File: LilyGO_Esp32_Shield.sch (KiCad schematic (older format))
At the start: 45 parts, among them J1 Conn. Flow4, J2 Conn. Flow3, J3 Conn. Flow2, J4 Conn. Flow1, J5 Conn. Pressure, J6 TEMP1, J7 TEMP2, SW1 SW_SPDT, U1 SN74HC14DR, U2 LilyGO_ESP32_TTGO

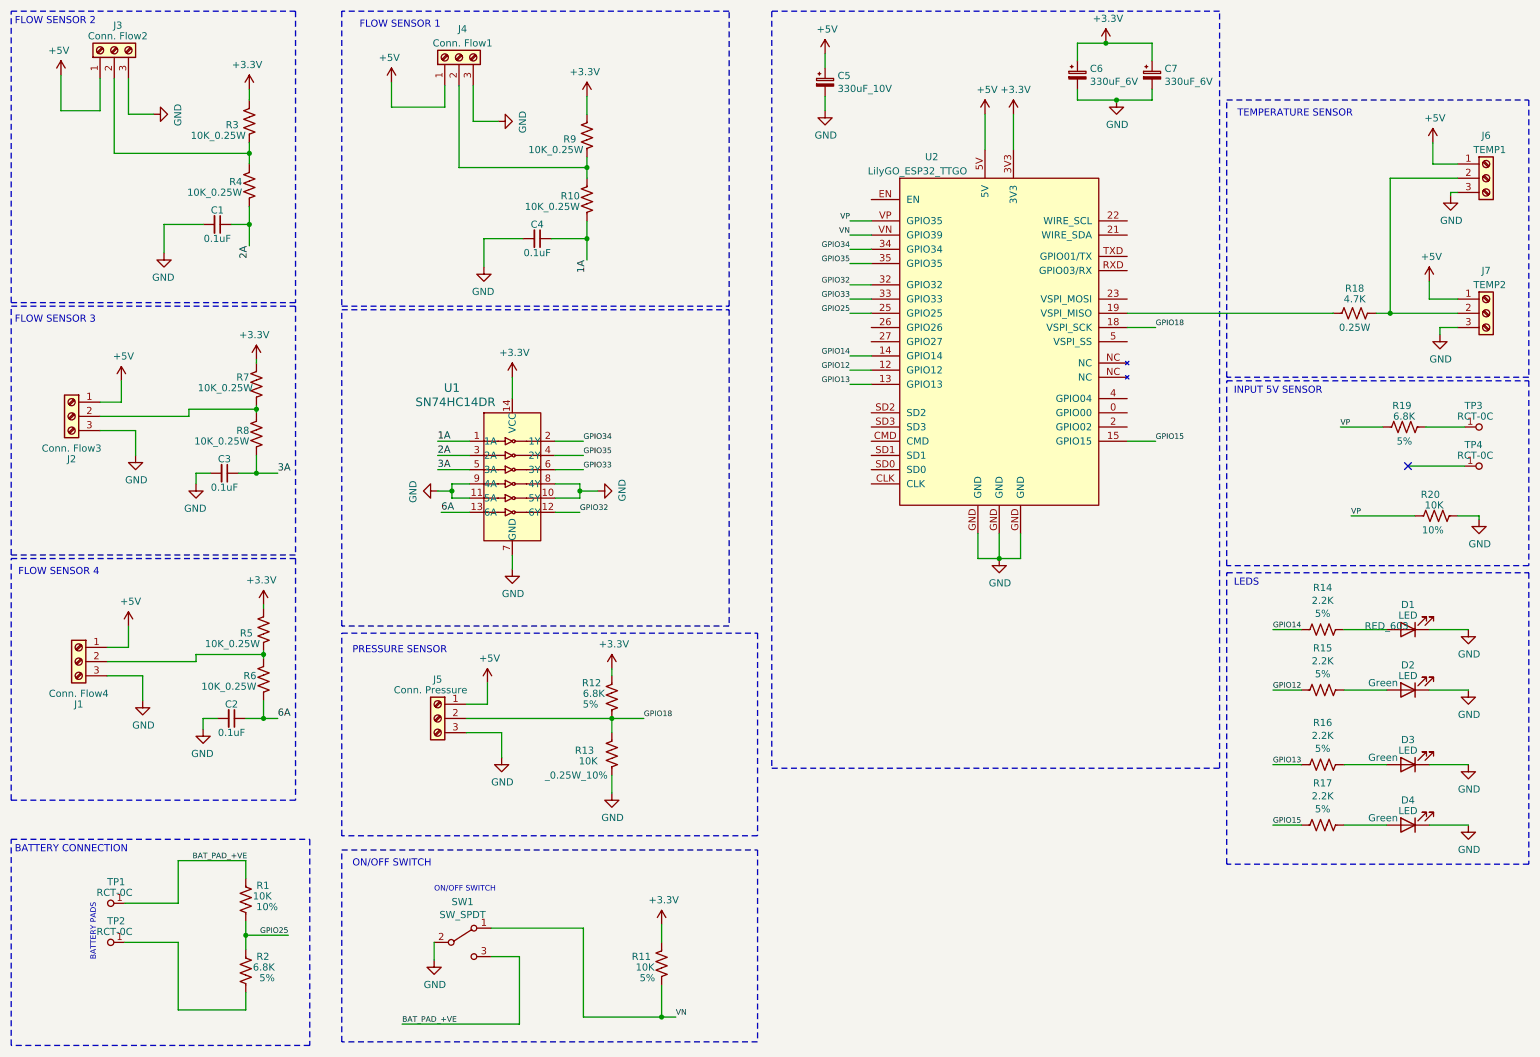
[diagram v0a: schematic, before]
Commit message: lily go footprint add
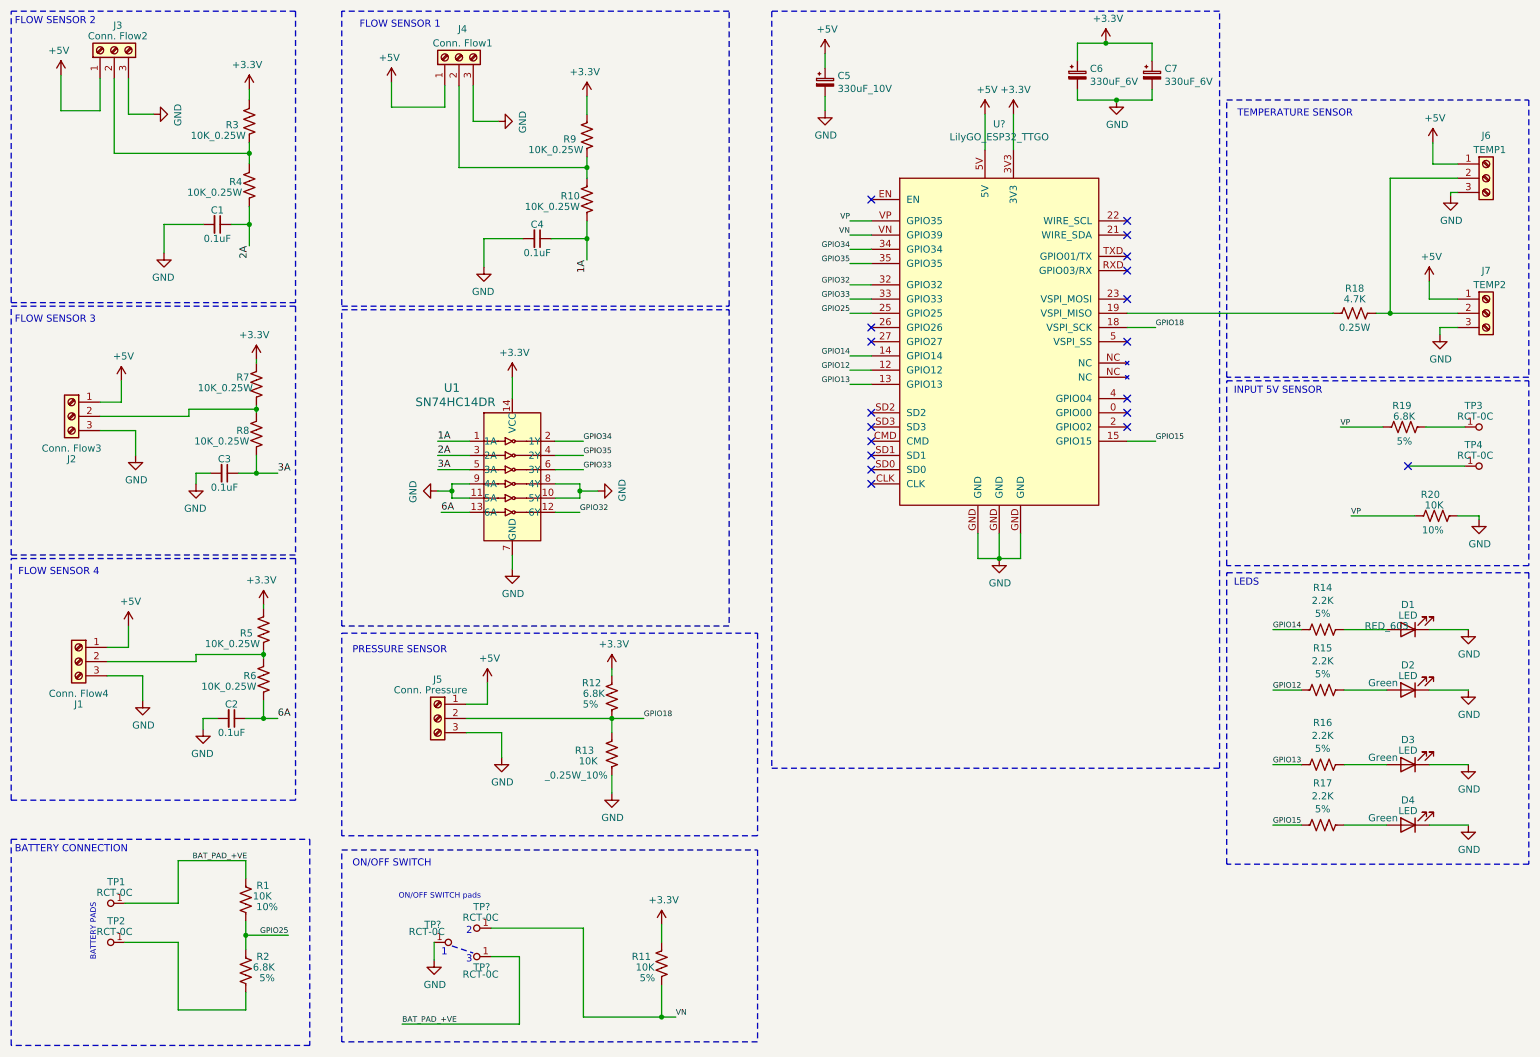
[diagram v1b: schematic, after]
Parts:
- removed SW1: SW_SPDT, symbol Switch:SW_SPDT
- removed U2: LilyGO_ESP32_TTGO, symbol GCL_Modules&Devboards:LilyGO_ESP32_TTGO
- added TP? (x3): RCT-0C, digikey-footprints:PROBE_PAD_1206, symbol dk_Test-Points:RCT-0C
- added U?: LilyGO_ESP32_TTGO, greencharge-footprints:LILLYGO_ESP32_TTGO, symbol GCL_Modules&Devboards:LilyGO_ESP32_TTGO
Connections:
- net +3V3: now also U?.3V3
- net +5V: now also U?.5V
- net BAT_PAD_+VE: now also TP?.1
- net GND: now also TP?.1, U?.GND
- net GPIO12: now also U?.12 (GPIO12)
- net GPIO13: now also U?.13 (GPIO13)
- net GPIO14: now also U?.14 (GPIO14)
- net GPIO15: now also U?.15 (GPIO15)
- net GPIO18: now also U?.18 (VSPI_SCK)
- net GPIO25: now also U?.25 (GPIO25)
- net GPIO32: now also U?.32 (GPIO32)
- net GPIO33: now also U?.33 (GPIO33)
- net GPIO34: now also U?.34 (GPIO34)
- net GPIO35: now also U?.35 (GPIO35)
- net VN: now also TP?.1, U?.VN (GPIO39)
- net VP: now also U?.VP (GPIO35)
- net at R18.2: now also U?.19 (VSPI_MISO)
- no-connect marks 1 -> 19
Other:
- note added: "1"
- note added: "2"
- note added: "3"
- note added: "ON/OFF SWITCH pads"
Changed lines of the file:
@@
 BATTERY PADS
-$Comp
-L Switch:SW_SPDT SW1
-U 1 1 61D13211
-P 3675 7050
-F 0 "SW1" H 3675 7335 50  0000 C CNN
-F 1 "SW_SPDT" H 3675 7244 50  0000 C CNN
-F 2 "" H 3675 7050 50  0001 C CNN
-F 3 "~" H 3675 7050 50  0001 C CNN
-	1    3675 7050
-	1    0    0    -1
-$EndComp
 $Comp
 L OLIMEX_Power:GND #PWR0125
@@
 Wire Wire Line
 	3475 7175 3475 7050
-Text Notes 3475 6700 0    39   ~ 0
-ON/OFF SWITCH
+Text Notes 3225 6750 0    39   ~ 0
+ON/OFF SWITCH pads
 Wire Wire Line
 	3875 7150 4075 7150
@@
 Wire Wire Line
 	8525 725  8200 725
-$Comp
-L GCL_Modules&Devboards:LilyGO_ESP32_TTGO U2
-U 1 1 61B0C159
-P 7450 1675
-F 0 "U2" H 6975 1825 50  0000 C CNN
-F 1 "LilyGO_ESP32_TTGO" H 6875 1725 50  0000 C CNN
-F 2 "" H 6500 1175 50  0001 C CNN
-F 3 "" H 6500 1175 50  0001 C CNN
-F 4 "LilyGO_ESP32_TTGO" H 7450 1675 50  0001 C CNN "MPN"
-	1    7450 1675
-	1    0    0    -1
-$EndComp
 Wire Wire Line
 	6550 2075 6400 2075
@@
 	1    0    0    -1
 $EndComp
+$Comp
+L GCL_Modules&Devboards:LilyGO_ESP32_TTGO U?
+U 1 1 61971A82
+P 7450 1675
+F 0 "U?" H 7450 2056 50  0000 C CNN
+F 1 "LilyGO_ESP32_TTGO" H 7450 1965 50  0000 C CNN
+F 2 "greencharge-footprints:LILLYGO_ESP32_TTGO" H 6500 1175 50  0001 C CNN
+F 3 "" H 6500 1175 50  0001 C CNN
+	1    7450 1675
+	1    0    0    -1
+$EndComp
+NoConn ~ 6550 1825
+NoConn ~ 6550 2725
+NoConn ~ 6550 2825
+NoConn ~ 6550 3325
+NoConn ~ 6550 3425
+NoConn ~ 6550 3525
+NoConn ~ 6550 3625
+NoConn ~ 6550 3725
+NoConn ~ 6550 3825
+NoConn ~ 8350 3425
+NoConn ~ 8350 3325
+NoConn ~ 8350 3225
+NoConn ~ 8350 2825
+NoConn ~ 8350 2525
+NoConn ~ 8350 2325
+NoConn ~ 8350 2225
+NoConn ~ 8350 2075
+NoConn ~ 8350 1975
+$Comp
+L dk_Test-Points:RCT-0C TP?
+U 1 1 61A05A6B
+P 3575 7050
+F 0 "TP?" V 3450 7100 50  0000 L CNN
+F 1 "RCT-0C" V 3500 7075 50  0000 L CNN
+F 2 "digikey-footprints:PROBE_PAD_1206" H 3775 7250 60  0001 L CNN
+F 3 "https://www.te.com/commerce/DocumentDelivery/DDEController?Action=srchrtrv&DocNm=1773266&DocType=DS&DocLang=English" H 3775 7350 60  0001 L CNN
+F 4 "A106144CT-ND" H 3775 7450 60  0001 L CNN "Digi-Key_PN"
+F 5 "RCT-0C" H 3775 7550 60  0001 L CNN "MPN"
+F 6 "Test and Measurement" H 3775 7650 60  0001 L CNN "Category"
+F 7 "Test Points" H 3775 7750 60  0001 L CNN "Family"
+F 8 "https://www.te.com/commerce/DocumentDelivery/DDEController?Action=srchrtrv&DocNm=1773266&DocType=DS&DocLang=English" H 3775 7850 60  0001 L CNN "DK_Datasheet_Link"
+F 9 "/product-detail/en/te-connectivity-amp-connectors/RCT-0C/A106144CT-ND/3477801" H 3775 7950 60  0001 L CNN "DK_Detail_Page"
+F 10 "PC TEST POINT NATURAL" H 3775 8050 60  0001 L CNN "Description"
+F 11 "TE Connectivity AMP Connectors" H 3775 8150 60  0001 L CNN "Manufacturer"
+F 12 "Active" H 3775 8250 60  0001 L CNN "Status"
+	1    3575 7050
+	0    -1   1    0
+$EndComp
+$Comp
+L dk_Test-Points:RCT-0C TP?
+U 1 1 61A1D60E
+P 3775 7150
+F 0 "TP?" V 3700 7125 50  0000 L CNN
+F 1 "RCT-0C" V 3650 7050 50  0000 L CNN
+F 2 "digikey-footprints:PROBE_PAD_1206" H 3975 7350 60  0001 L CNN
+F 3 "https://www.te.com/commerce/DocumentDelivery/DDEController?Action=srchrtrv&DocNm=1773266&DocType=DS&DocLang=English" H 3975 7450 60  0001 L CNN
+F 4 "A106144CT-ND" H 3975 7550 60  0001 L CNN "Digi-Key_PN"
+F 5 "RCT-0C" H 3975 7650 60  0001 L CNN "MPN"
+F 6 "Test and Measurement" H 3975 7750 60  0001 L CNN "Category"
+F 7 "Test Points" H 3975 7850 60  0001 L CNN "Family"
+F 8 "https://www.te.com/commerce/DocumentDelivery/DDEController?Action=srchrtrv&DocNm=1773266&DocType=DS&DocLang=English" H 3975 7950 60  0001 L CNN "DK_Datasheet_Link"
+F 9 "/product-detail/en/te-connectivity-amp-connectors/RCT-0C/A106144CT-ND/3477801" H 3975 8050 60  0001 L CNN "DK_Detail_Page"
+F 10 "PC TEST POINT NATURAL" H 3975 8150 60  0001 L CNN "Description"
+F 11 "TE Connectivity AMP Connectors" H 3975 8250 60  0001 L CNN "Manufacturer"
+F 12 "Active" H 3975 8350 60  0001 L CNN "Status"
+	1    3775 7150
+	0    1    -1   0
+$EndComp
+$Comp
+L dk_Test-Points:RCT-0C TP?
+U 1 1 61A156F3
+P 3775 6950
+F 0 "TP?" V 3925 6925 50  0000 L CNN
+F 1 "RCT-0C" V 3850 6850 50  0000 L CNN
+F 2 "digikey-footprints:PROBE_PAD_1206" H 3975 7150 60  0001 L CNN
+F 3 "https://www.te.com/commerce/DocumentDelivery/DDEController?Action=srchrtrv&DocNm=1773266&DocType=DS&DocLang=English" H 3975 7250 60  0001 L CNN
+F 4 "A106144CT-ND" H 3975 7350 60  0001 L CNN "Digi-Key_PN"
+F 5 "RCT-0C" H 3975 7450 60  0001 L CNN "MPN"
+F 6 "Test and Measurement" H 3975 7550 60  0001 L CNN "Category"
+F 7 "Test Points" H 3975 7650 60  0001 L CNN "Family"
+F 8 "https://www.te.com/commerce/DocumentDelivery/DDEController?Action=srchrtrv&DocNm=1773266&DocType=DS&DocLang=English" H 3975 7750 60  0001 L CNN "DK_Datasheet_Link"
+F 9 "/product-detail/en/te-connectivity-amp-connectors/RCT-0C/A106144CT-ND/3477801" H 3975 7850 60  0001 L CNN "DK_Detail_Page"
+F 10 "PC TEST POINT NATURAL" H 3975 7950 60  0001 L CNN "Description"
+F 11 "TE Connectivity AMP Connectors" H 3975 8050 60  0001 L CNN "Manufacturer"
+F 12 "Active" H 3975 8150 60  0001 L CNN "Status"
+	1    3775 6950
+	0    1    -1   0
+$EndComp
+Text Notes 3525 7150 0    50   ~ 0
+1
+Text Notes 3700 7000 0    50   ~ 0
+2
+Text Notes 3700 7200 0    50   ~ 0
+3
+Wire Notes Line
+	3600 7075 3750 7125
 $EndSCHEMATC
